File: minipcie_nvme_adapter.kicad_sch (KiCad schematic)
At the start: 2 parts, among them J1 Bus_PCI_Express_Mini, J2 Bus_M.2_Socket_M

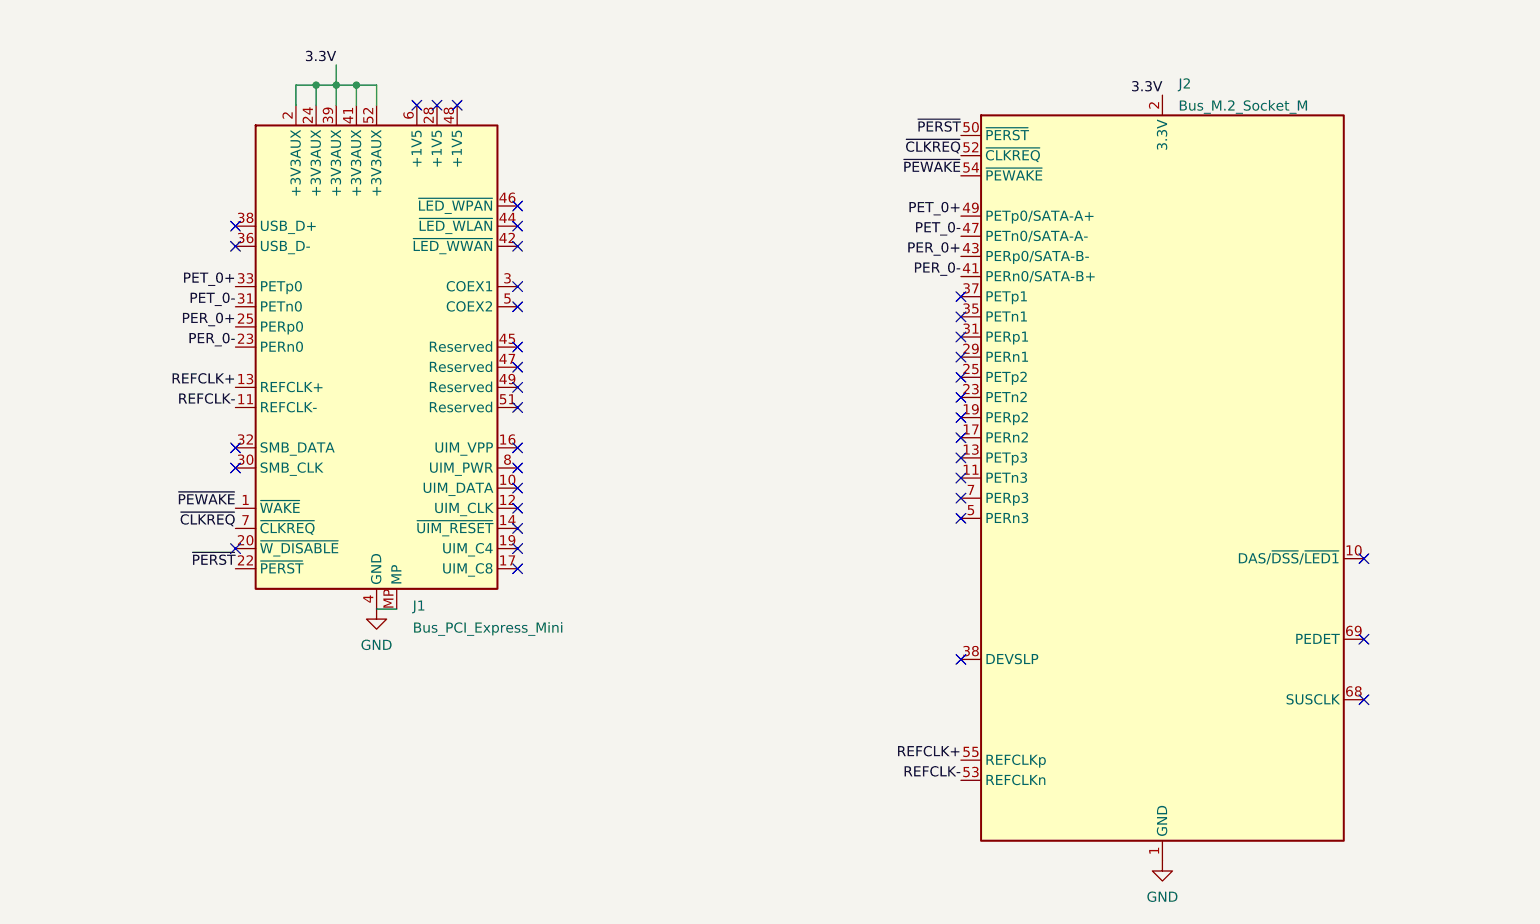
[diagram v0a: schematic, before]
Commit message: Move m.2 connector right so that we can fit up to 2280 cards without exceeding 100mm width
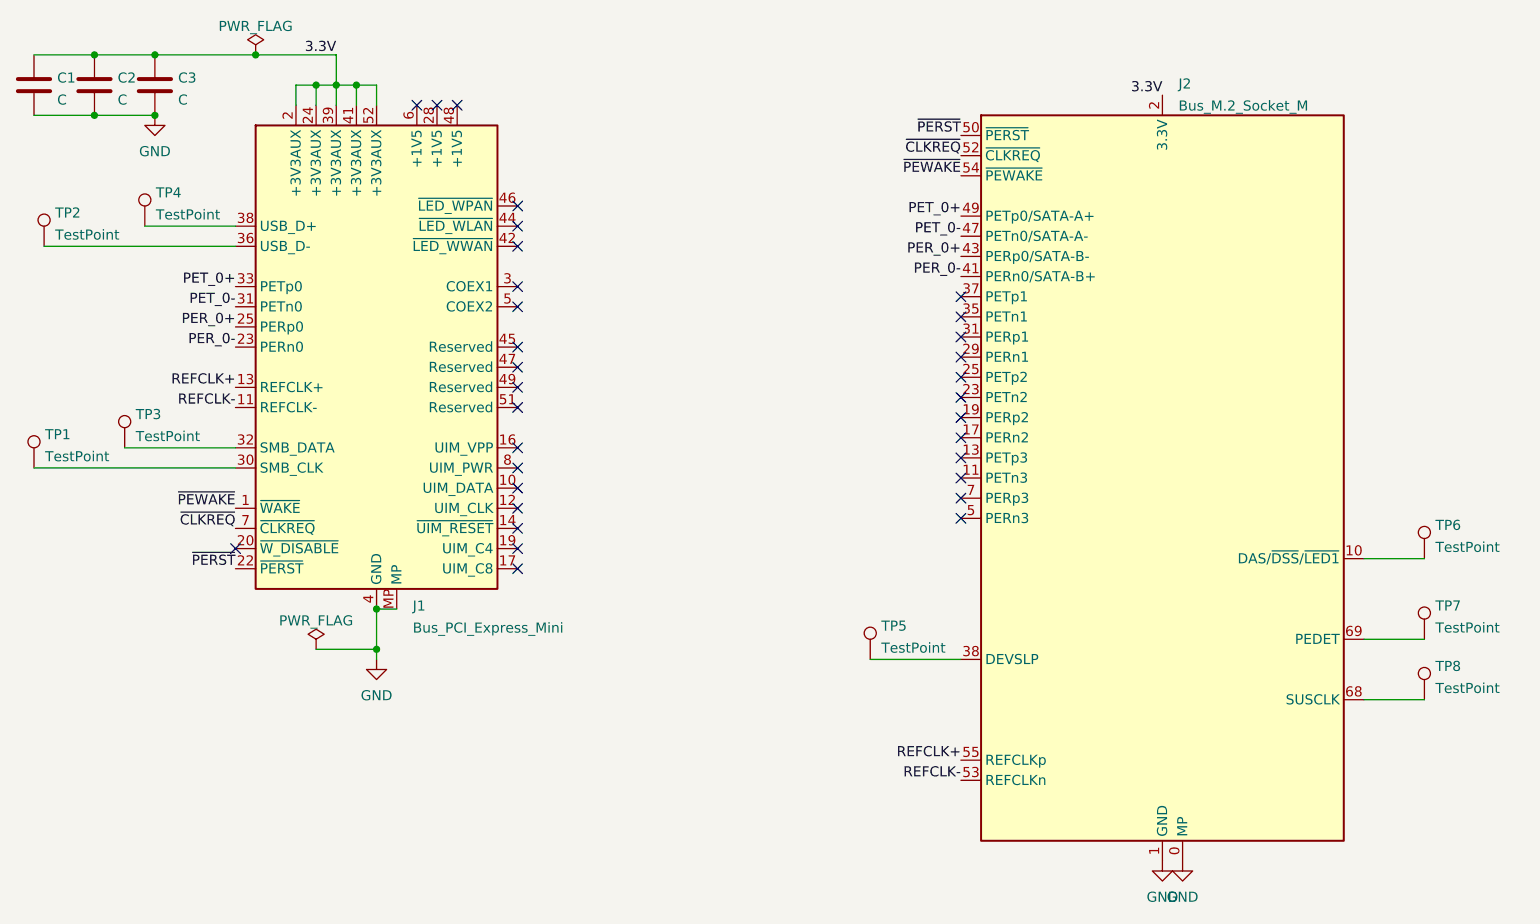
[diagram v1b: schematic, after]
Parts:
- added C1: C, Capacitor_SMD:C_0805_2012Metric, symbol Device:C
- added C2, C3: C, Capacitor_SMD:C_0402_1005Metric, symbol Device:C
- added TP1, TP2, TP3, TP4, TP5, TP6, TP7, TP8: TestPoint, TestPoint:TestPoint_Pad_1.0x1.0mm, symbol Connector:TestPoint
- J2: JLCPCB (none) -> C841645
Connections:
- net 3.3V: now also C1.1, C2.1, C3.1
- net GND: now also J2.0 (MP), C1.2, C2.2, C3.2
- net at J1.30 (SMB_CLK): now also TP1.1
- net at J1.32 (SMB_DATA): now also TP3.1
- net at J1.36 (USB_D-): now also TP2.1
- net at J1.38 (USB_D+): now also TP4.1
- net at J2.10 (DAS/~{DSS}/~{LED1}): now also TP6.1
- net at J2.38 (DEVSLP): now also TP5.1
- net at J2.68 (SUSCLK): now also TP8.1
- net at J2.69 (PEDET): now also TP7.1
- no-connect marks 40 -> 32
